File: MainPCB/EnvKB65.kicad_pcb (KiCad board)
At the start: 2 copper layers, 320.8 x 99.3 mm, 148 parts, among them U1 Pico

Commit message: Swapped out mechboads logo for personal order
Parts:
- Ref**: footprint MechboardsLogo:mechboardsLOGO_20mm -> Logo:logo
- moved Ref** 1.10 mm to (367.6, 155.0)
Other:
- board text removed: "http://Mechboards.co.uk"

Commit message: Added ANSI support, generated Gerbers and sent to JLCPCB
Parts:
- removed the K_63 at (74.9, 187.7)
- added D_27: Diode SOD-323, Diode_SMD:D_SOD-323_HandSoldering, B.Cu at (321.5, 137.6)
- added K_27: KEYSW, MX_Only:MXOnly-1.5U-NoLED, F.Cu at (334.4, 130.6)
- added K_28: KEYSW, MX_Only:MXOnly-2.25U-NoLED, F.Cu at (327.3, 149.6)
- added K_43: KEYSW, MX_Only:MXOnly-2.25U-NoLED, F.Cu at (84.4, 168.7)
- added K_60: KEYSW, MX_Only:MXOnly-1.25U-NoLED, F.Cu at (74.9, 187.7)
- D_0, D_1, D_10, D_11, D_12, D_13, D_2, D_3, D_4, D_5, D_6, D_7, D_8, D_9: value D -> Diode SOD-323
- D_14: renamed from D_16; value D -> Diode SOD-323
- D_15: renamed from D_17; value D -> Diode SOD-323
- D_16: renamed from D_18; value D -> Diode SOD-323
- D_17: renamed from D_19; value D -> Diode SOD-323
- D_18: renamed from D_20; value D -> Diode SOD-323
- D_19: renamed from D_21; value D -> Diode SOD-323
- D_20: renamed from D_22; value D -> Diode SOD-323
- D_21: renamed from D_23; value D -> Diode SOD-323
- D_22: renamed from D_24; value D -> Diode SOD-323
- D_23: renamed from D_25; value D -> Diode SOD-323
- D_24: renamed from D_26; value D -> Diode SOD-323
- D_25: renamed from D_27; value D -> Diode SOD-323
- D_26: renamed from D_28; value D -> Diode SOD-323
- D_28: renamed from D_32; value D -> Diode SOD-323
- D_29: renamed from D_33; value D -> Diode SOD-323
- D_30: renamed from D_34; value D -> Diode SOD-323
- D_31: renamed from D_35; value D -> Diode SOD-323
- D_32: renamed from D_36; value D -> Diode SOD-323
- D_33: renamed from D_37; value D -> Diode SOD-323
- D_34: renamed from D_38; value D -> Diode SOD-323
- D_35: renamed from D_39; value D -> Diode SOD-323
- D_36: renamed from D_40; value D -> Diode SOD-323
- D_37: renamed from D_41; value D -> Diode SOD-323
- D_38: renamed from D_42; value D -> Diode SOD-323
- D_39: renamed from D_43; value D -> Diode SOD-323
- D_40: renamed from D_44; value D -> Diode SOD-323
- D_41: renamed from D_29; value D -> Diode SOD-323
- D_42: renamed from D_47; value D -> Diode SOD-323
- D_43: renamed from D_48; value D -> Diode SOD-323
- D_44: renamed from D_49; value D -> Diode SOD-323
- D_45: renamed from D_50; value D -> Diode SOD-323
- D_46: renamed from D_51; value D -> Diode SOD-323
- D_47: renamed from D_52; value D -> Diode SOD-323
- D_48: renamed from D_53; value D -> Diode SOD-323
- D_49: renamed from D_54; value D -> Diode SOD-323
- D_50: renamed from D_55; value D -> Diode SOD-323
- D_51: renamed from D_56; value D -> Diode SOD-323
- D_52: renamed from D_57; value D -> Diode SOD-323
- D_53: renamed from D_58; value D -> Diode SOD-323
- D_54: renamed from D_59; value D -> Diode SOD-323
- D_55: renamed from D_60; value D -> Diode SOD-323
- D_56: renamed from D_61; value D -> Diode SOD-323
- D_57: renamed from D_62; value D -> Diode SOD-323
- D_58: renamed from D_63; value D -> Diode SOD-323
- D_59: renamed from D_64; value D -> Diode SOD-323
- D_60: renamed from D_65; value D -> Diode SOD-323
- D_61: renamed from D_66; value D -> Diode SOD-323
- D_62: renamed from D_67; value D -> Diode SOD-323
- D_63: renamed from D_68; value D -> Diode SOD-323
- D_64: renamed from D_69; value D -> Diode SOD-323
- D_65: renamed from D_70; value D -> Diode SOD-323
- D_66: renamed from D_71; value D -> Diode SOD-323
- D_67: renamed from D_72; value D -> Diode SOD-323
- D_68: renamed from D_73; value D -> Diode SOD-323
- D_69: renamed from D_74; value D -> Diode SOD-323
- D_70: renamed from D_75; value D -> Diode SOD-323
- moved H2 17.7 mm to (86.8, 185.2)
- renumbered H1 to H0, H2 to H1, H3 to H2, H4 to H3, H5 to H4, H6 to H5, K_16 to K_14, K_17 to K_15, K_18 to K_16, K_19 to K_17, K_20 to K_18, K_21 to K_19, K_22 to K_20, K_23 to K_21, K_24 to K_22, K_25 to K_23, K_26 to K_24, K_27 to K_25, K_28 to K_26, K_32 to K_29, K_33 to K_30, K_34 to K_31, K_35 to K_32, K_36 to K_33, K_37 to K_34, K_38 to K_35, K_39 to K_36, K_40 to K_37, K_41 to K_38, K_42 to K_39, K_43 to K_40, K_44 to K_41, K_29 to K_42, K_47 to K_44, K_48 to K_45, K_49 to K_46, K_50 to K_47, K_51 to K_48, K_52 to K_49, K_53 to K_50, K_54 to K_51, K_55 to K_52, K_56 to K_53, K_57 to K_54, K_58 to K_55, K_59 to K_56, K_60 to K_57, K_61 to K_58, K_62 to K_59, K_64 to K_61, K_65 to K_62, K_66 to K_63, K_67 to K_64, K_68 to K_65, K_69 to K_66, K_70 to K_67, K_71 to K_68, K_72 to K_69, K_73 to K_70, K_74 to K_71, K_75 to K_72, U1 to U0
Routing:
- net col14: track 104.2 -> 140.7 mm
- net Net-(D_27-Pad2): track 0.00 -> 24.9 mm
- net Net-(D_41-Pad2): track 14.5 -> 31.4 mm
- net col0: track 380.4 -> 389.5 mm
- net Net-(D_42-Pad2): track 14.6 -> 22.7 mm
- net row2: track 309.5 -> 315.2 mm
- net row3: track 343.0 -> 345.9 mm
- net Net-(D_40-Pad2): track 13.3 -> 14.8 mm
- net row1: track 327.0 -> 326.2 mm

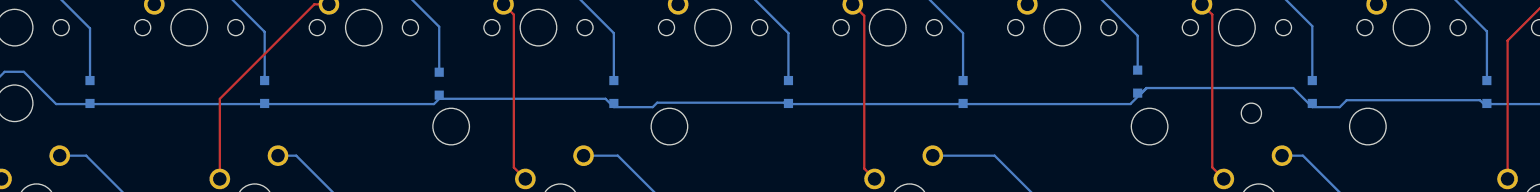
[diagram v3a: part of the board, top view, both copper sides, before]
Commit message: corrected a couple silkscreen issues and moved some traces further from some holes.
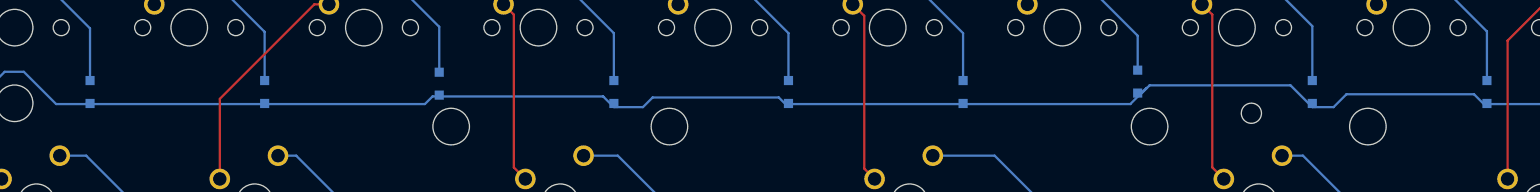
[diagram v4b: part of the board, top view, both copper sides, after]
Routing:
- net row3: track 345.9 -> 347.5 mm
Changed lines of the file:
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@@
     (thickness 1.6)
     (drawings 640)
-    (tracks 688)
+    (tracks 692)
     (zones 0)
     (modules 152)
@@
     (tags SOD-323)
     (attr smd)
-    (fp_text reference D_26 (at 0 1.85 90) (layer B.SilkS)
+    (fp_text reference D_26 (at 0 -1.8992 90) (layer B.SilkS)
       (effects (font (size 1 1) (thickness 0.15)) (justify mirror))
     )
@@
   (segment (start 373.52 157.47) (end 373.52 142.81) (width 0.25) (layer B.Cu) (net 21))
   (segment (start 373.52 157.47) (end 373.52 157.22) (width 0.25) (layer B.Cu) (net 21))
-  (segment (start 85.4967 177.33412) (end 85.83082 177) (width 0.25) (layer B.Cu) (net 21))
-  (segment (start 161.6967 177.33412) (end 165.94088 177.33412) (width 0.25) (layer B.Cu) (net 21))
-  (segment (start 180.41258 177) (end 218.0467 177) (width 0.25) (layer B.Cu) (net 21))
-  (segment (start 142.0717 177) (end 142.6467 176.425) (width 0.25) (layer B.Cu) (net 21))
-  (segment (start 165.94088 177.33412) (end 166.425 176.85) (width 0.25) (layer B.Cu) (net 21))
-  (segment (start 142.6467 176.425) (end 160.78758 176.425) (width 0.25) (layer B.Cu) (net 21))
-  (segment (start 160.78758 176.425) (end 161.6967 177.33412) (width 0.25) (layer B.Cu) (net 21))
-  (segment (start 166.425 176.85) (end 180.26258 176.85) (width 0.25) (layer B.Cu) (net 21))
-  (segment (start 180.26258 176.85) (end 180.41258 177) (width 0.25) (layer B.Cu) (net 21))
-  (segment (start 218.0467 177) (end 219.7967 175.25) (width 0.25) (layer B.Cu) (net 21))
   (segment (start 218.8467 175.8) (end 219.3 175.8) (width 0.25) (layer B.Cu) (net 21))
   (segment (start 219.3 175.8) (end 219.85 175.25) (width 0.25) (layer B.Cu) (net 21))
-  (segment (start 219.7967 175.25) (end 219.85 175.25) (width 0.25) (layer B.Cu) (net 21))
-  (segment (start 256.61258 177) (end 369.08176 177) (width 0.25) (layer B.Cu) (net 21))
-  (segment (start 256.18758 176.575) (end 256.61258 177) (width 0.25) (layer B.Cu) (net 21))
-  (segment (start 240.89088 177.33412) (end 241.65 176.575) (width 0.25) (layer B.Cu) (net 21))
-  (segment (start 237.8967 177.33412) (end 240.89088 177.33412) (width 0.25) (layer B.Cu) (net 21))
-  (segment (start 241.65 176.575) (end 256.18758 176.575) (width 0.25) (layer B.Cu) (net 21))
-  (segment (start 235.81258 175.25) (end 237.8967 177.33412) (width 0.25) (layer B.Cu) (net 21))
-  (segment (start 219.85 175.25) (end 235.81258 175.25) (width 0.25) (layer B.Cu) (net 21))
   (segment (start 373.52 158.33) (end 373.52 157.47) (width 0.25) (layer B.Cu) (net 21))
   (segment (start 381.29 161.43) (end 376.62 161.43) (width 0.25) (layer B.Cu) (net 21))
@@
   (segment (start 369.25 177) (end 377.26824 177) (width 0.25) (layer B.Cu) (net 21))
   (segment (start 376.62 161.43) (end 373.52 158.33) (width 0.25) (layer B.Cu) (net 21))
-  (segment (start 91.74 177) (end 91.74 176.98) (width 0.25) (layer B.Cu) (net 21))
+  (segment (start 180.41258 177) (end 218.0467 177) (width 0.25) (layer B.Cu) (net 21))
+  (segment (start 161.6967 177.33412) (end 164.86988 177.33412) (width 0.25) (layer B.Cu) (net 21))
   (segment (start 85.83082 177) (end 91.74 177) (width 0.25) (layer B.Cu) (net 21))
+  (segment (start 91.74 177) (end 91.74 176.98) (width 0.25) (layer B.Cu) (net 21))
+  (segment (start 141.081 177) (end 141.915 176.166) (width 0.25) (layer B.Cu) (net 21))
   (segment (start 91.74 176.98) (end 95.24 173.48) (width 0.25) (layer B.Cu) (net 21))
-  (segment (start 97.33 173.48) (end 100.85 177) (width 0.25) (layer B.Cu) (net 21))
+  (segment (start 218.0467 177) (end 219.7967 175.25) (width 0.25) (layer B.Cu) (net 21))
   (segment (start 95.24 173.48) (end 97.33 173.48) (width 0.25) (layer B.Cu) (net 21))
-  (segment (start 100.85 177) (end 142.0717 177) (width 0.25) (layer B.Cu) (net 21))
+  (segment (start 97.33 173.48) (end 100.85 177) (width 0.25) (layer B.Cu) (net 21))
+  (segment (start 179.69458 176.282) (end 180.41258 177) (width 0.25) (layer B.Cu) (net 21))
+  (segment (start 100.85 177) (end 141.081 177) (width 0.25) (layer B.Cu) (net 21))
+  (segment (start 165.922 176.282) (end 179.69458 176.282) (width 0.25) (layer B.Cu) (net 21))
+  (segment (start 219.7967 175.25) (end 219.85 175.25) (width 0.25) (layer B.Cu) (net 21))
+  (segment (start 85.4967 177.33412) (end 85.83082 177) (width 0.25) (layer B.Cu) (net 21))
+  (segment (start 160.52858 176.166) (end 161.6967 177.33412) (width 0.25) (layer B.Cu) (net 21))
+  (segment (start 164.86988 177.33412) (end 165.922 176.282) (width 0.25) (layer B.Cu) (net 21))
+  (segment (start 142.6467 176.1163) (end 142.597 176.166) (width 0.25) (layer B.Cu) (net 21))
+  (segment (start 142.597 176.166) (end 160.52858 176.166) (width 0.25) (layer B.Cu) (net 21))
+  (segment (start 142.6467 176.025) (end 142.6467 176.1163) (width 0.25) (layer B.Cu) (net 21))
+  (segment (start 141.915 176.166) (end 142.597 176.166) (width 0.25) (layer B.Cu) (net 21))
+  (segment (start 256.61258 177) (end 369.08176 177) (width 0.25) (layer B.Cu) (net 21))
+  (segment (start 255.54058 175.928) (end 256.61258 177) (width 0.25) (layer B.Cu) (net 21))
+  (segment (start 241.621 175.928) (end 255.54058 175.928) (width 0.25) (layer B.Cu) (net 21))
+  (segment (start 237.8967 177.33412) (end 240.21488 177.33412) (width 0.25) (layer B.Cu) (net 21))
+  (segment (start 235.51958 174.957) (end 237.8967 177.33412) (width 0.25) (layer B.Cu) (net 21))
+  (segment (start 240.21488 177.33412) (end 241.621 175.928) (width 0.25) (layer B.Cu) (net 21))
+  (segment (start 220.143 174.957) (end 235.51958 174.957) (width 0.25) (layer B.Cu) (net 21))
+  (segment (start 219.85 175.25) (end 220.143 174.957) (width 0.25) (layer B.Cu) (net 21))
   (segment (start 366.3342 191.85912) (end 366.59332 191.6) (width 0.25) (layer B.Cu) (net 22))
   (segment (start 374.17001 147.23999) (end 376.67 144.74) (width 0.25) (layer B.Cu) (net 22))

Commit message: Mount hole tweak to allow for switches to seat properly with a spacer installed
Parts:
- removed Ref**: Val**, Logo:logo
- moved H5 21.6 mm to (210.6, 184.5)
- moved H4 0.68 mm to (224.9, 121.8)
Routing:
- net row2: track 315.2 -> 316.7 mm
- net col0: track 389.5 -> 388.0 mm
- net row0: track 353.5 -> 354.2 mm

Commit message: moved some mount holes a tiny bit and adjusted some traces for wider clearance.
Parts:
- moved D_56 3.19 mm to (366.4, 172.5)
- moved D_57 3.19 mm to (369.2, 172.5)
- moved H3 2.30 mm to (367.8, 178.2)
- moved H4 0.23 mm to (224.9, 121.6)
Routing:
- net row1: track 326.2 -> 329.3 mm
- net row3: track 347.5 -> 350.2 mm
- net Net-(D_56-Pad2): track 13.8 -> 11.2 mm
- net Net-(D_57-Pad2): track 20.3 -> 17.7 mm
- net row2: track 316.7 -> 314.4 mm
- net row0: track 354.2 -> 353.4 mm

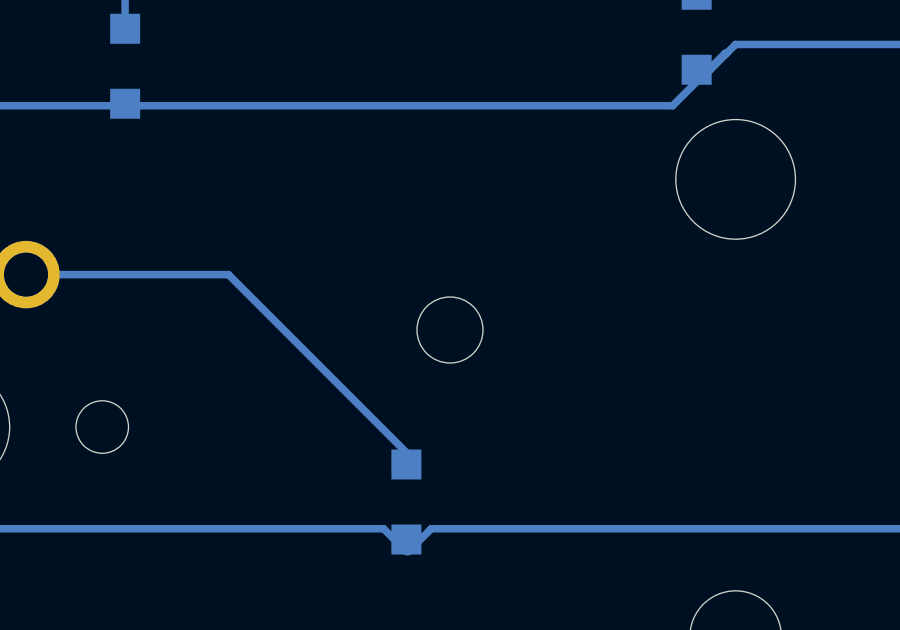
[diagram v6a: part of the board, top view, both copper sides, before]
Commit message: moved mount hole#6 up by 1mm and changed stabilizer cut out.
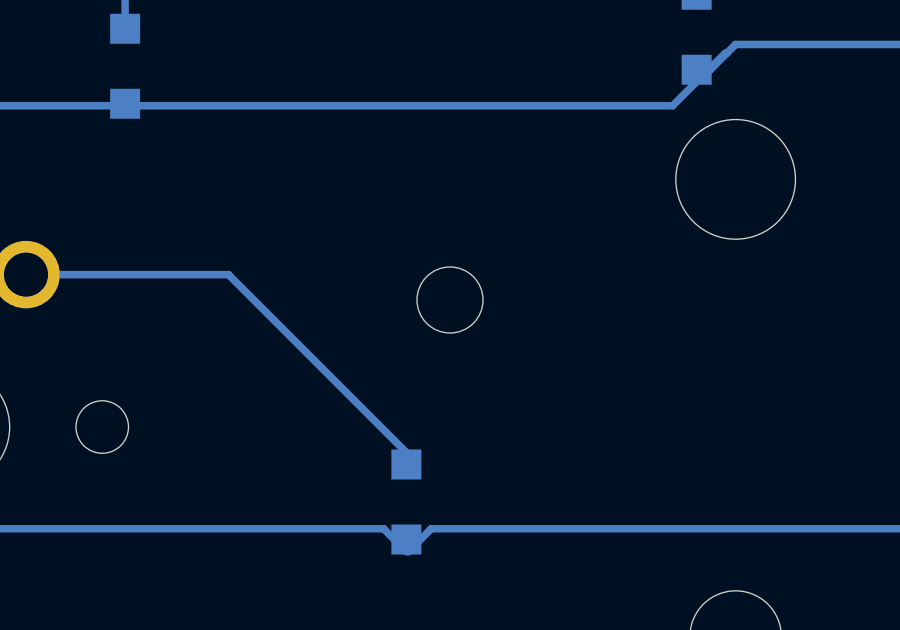
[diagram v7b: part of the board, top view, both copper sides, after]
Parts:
- moved H5 1.00 mm to (210.6, 183.5)

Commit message: Cleaned up a couple strange mistakes.
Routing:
- net row1: track 329.3 -> 324.2 mm
- net gnd: track 2.59 -> 0.00 mm
- net col0: track 388.0 -> 389.0 mm
- net col13: track 153.6 -> 154.3 mm
- net col14: track 140.7 -> 140.1 mm
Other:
- board text added: "http://github.com/Envious-Data/Env-KB65M"
